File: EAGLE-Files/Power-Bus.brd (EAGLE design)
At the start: 36.8 x 9.8 mm, 13 parts

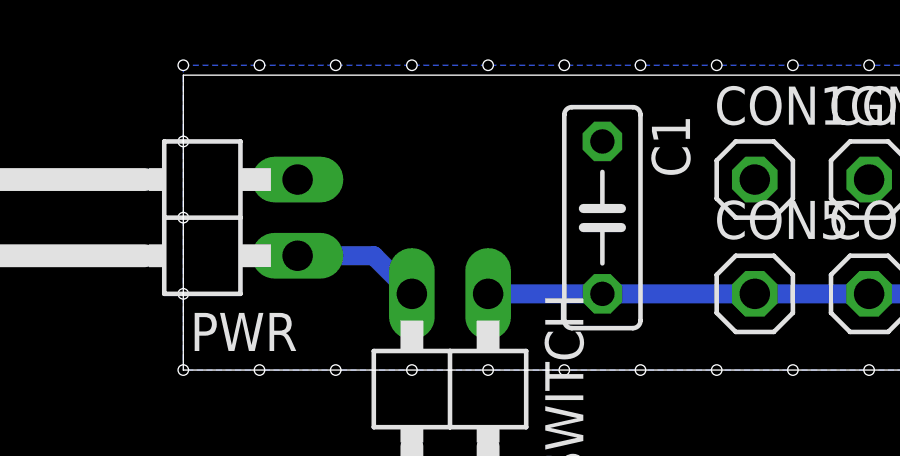
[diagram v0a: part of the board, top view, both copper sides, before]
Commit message: * Updated gitignore * Updated some of the EAGLE boards
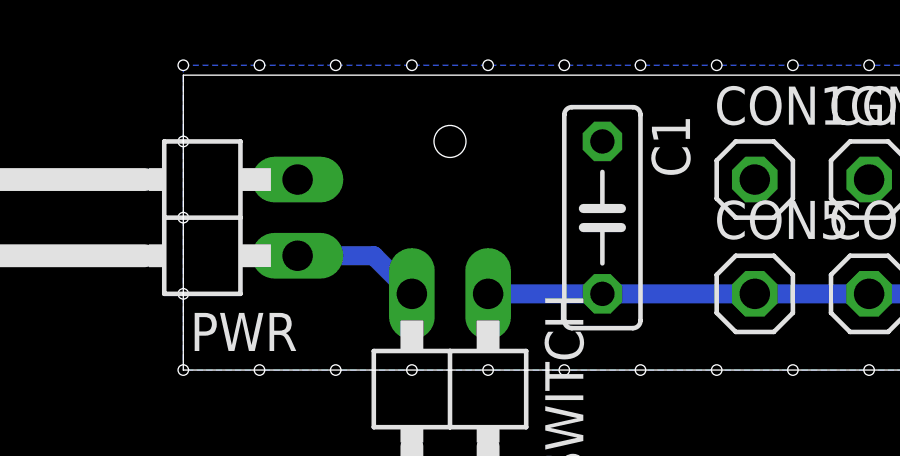
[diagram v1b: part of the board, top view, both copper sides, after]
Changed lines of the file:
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@@
 <hole x="36.83" y="6.35" drill="0.35"/>
 <hole x="36.83" y="8.89" drill="0.35"/>
+<hole x="8.89" y="7.62" drill="1.0668"/>
 </plain>
 <attributes>
